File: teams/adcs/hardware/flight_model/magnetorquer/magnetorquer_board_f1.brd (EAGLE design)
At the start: 90 x 90 mm, 35 parts, among them U5 LTC3624

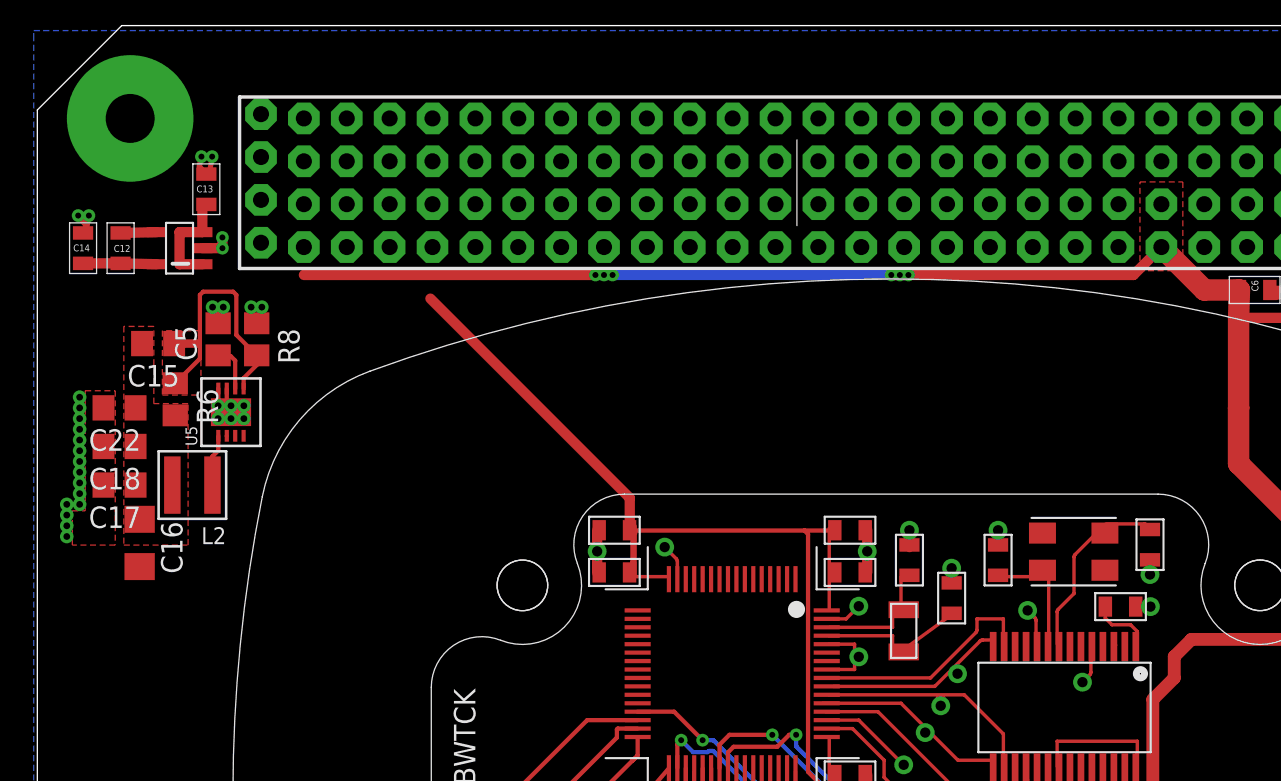
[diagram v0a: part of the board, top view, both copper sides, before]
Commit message: ADCS/MT: Reconnect CAN
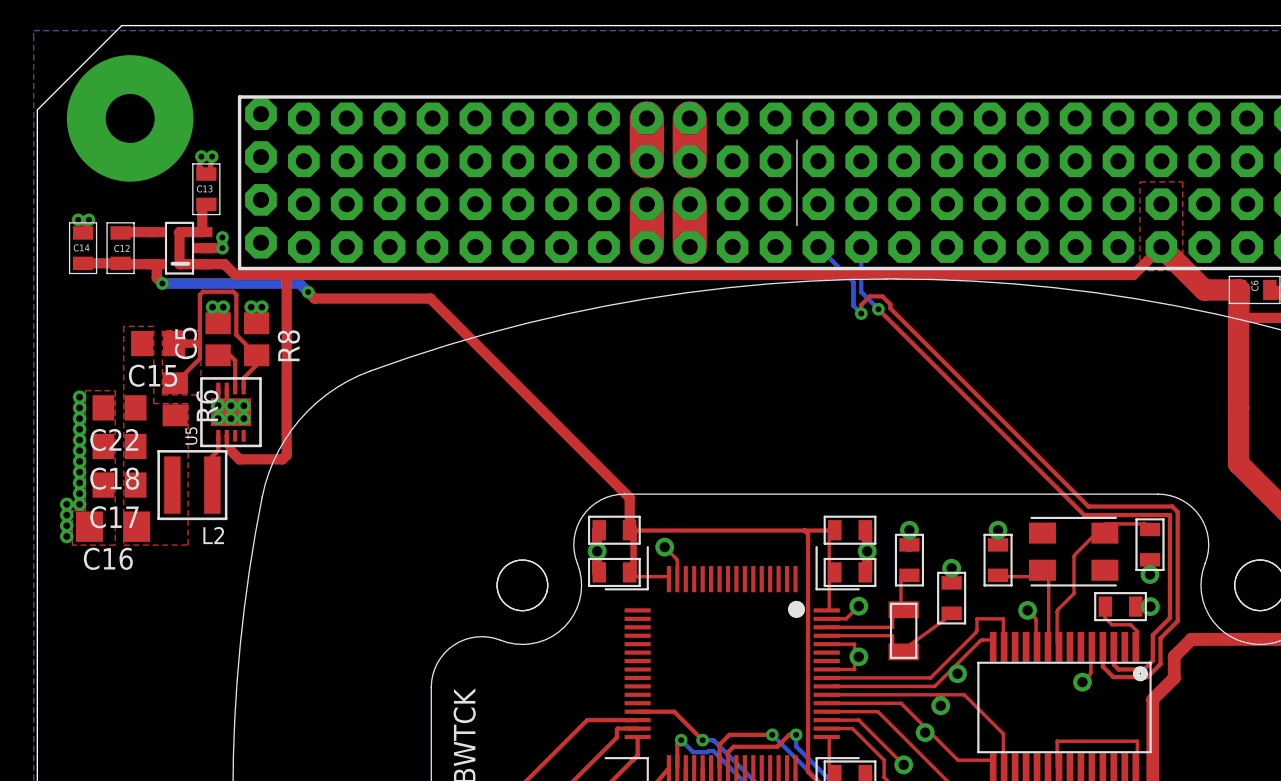
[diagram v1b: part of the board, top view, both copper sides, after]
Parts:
- moved C16 1.85 mm to (15.9, 59.0), turned to 180 degrees
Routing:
- net CANH: track 0.00 -> 44.5 mm, vias 0 -> 1
- net CANL: track 0.12 -> 39.3 mm, vias 0 -> 1
- net VBAT: track 110.9 -> 130.4 mm, vias 14 -> 8
- net +3V3: track 68.3 -> 85.8 mm, vias 0 -> 2
- net MT_Y_B: track 0.00 -> 2.54 mm
- net MT_Y_A: track 0.00 -> 2.54 mm
- net MT_X_B: track 0.00 -> 2.54 mm
- net MT_X_A: track 0.00 -> 2.54 mm

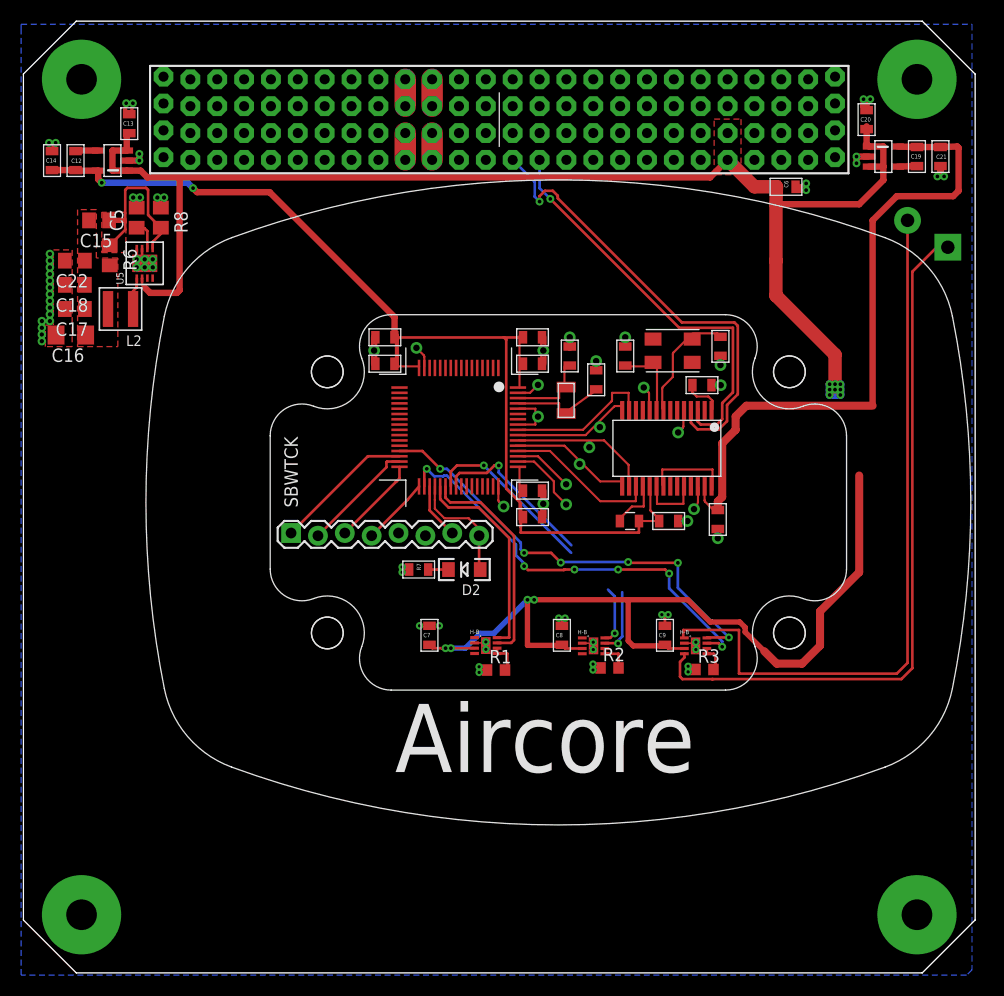
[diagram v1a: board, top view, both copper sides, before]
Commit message: ADCS/MT: Properly connect buck converter and reposition smoothing capacitors on H-Bridge
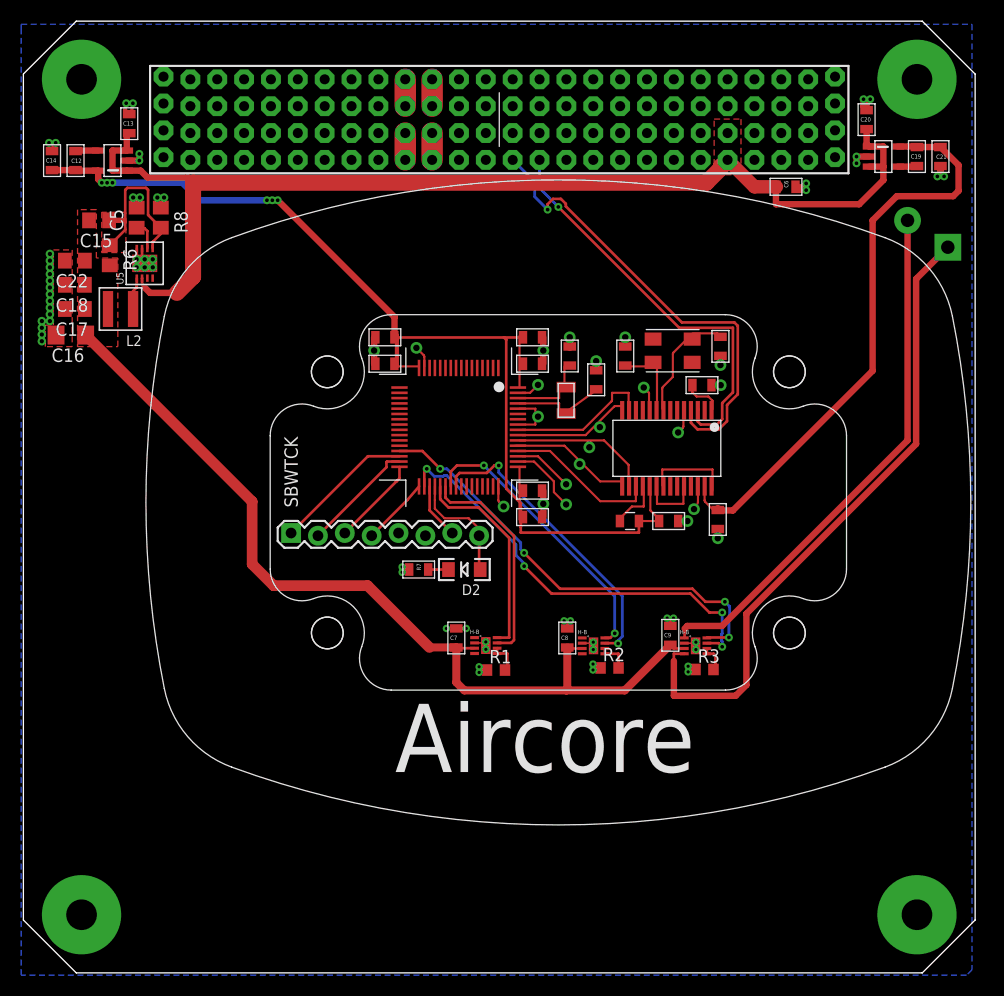
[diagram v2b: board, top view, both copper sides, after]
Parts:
- moved C7 2.55 mm to (52.3, 30.4)
- moved C8 0.57 mm to (62.8, 30.4)
- moved C9 0.51 mm to (72.6, 30.6)
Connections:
- removed net 3V3_BUCK_VOUT: C15.2, C16.1, C17.1, C18.1, C22.1, L2.P$2, R6.2
- net V_TORQ: now also C15.2, C16.1, C17.1, C18.1, C22.1, L2.P$2, R6.2
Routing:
- net VBAT: track 130.4 -> 106.3 mm, vias 8 -> 0
- net MT_Z_B: track 68.2 -> 50.2 mm
- net +5V: track 59.5 -> 52.8 mm
- net PWM_X_1: track 22.1 -> 28.5 mm
- net PWM_X_2: track 21.9 -> 26.9 mm
- net MT_Z_A: track 65.8 -> 61.6 mm
- net V_TORQ: track 82.2 -> 85.3 mm, vias 4 -> 0
- net PWM_Z_1: track 40.2 -> 41.0 mm, vias 6 -> 4
- net PWM_Z_2: track 42.4 -> 42.8 mm, vias 6 -> 4
- net +3V3: vias 2 -> 6
- added copper zone on layer 1, net V_TORQ
- removed copper zone on layer 1, net 3V3_BUCK_VOUT

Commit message: PC104 connector change: switched X and Y pin assignments, MQT board: converted to 4 layer board, layer 4 GND, previous layer 2 traces moved to new layer 2; added X and Y MQT outputs; added 3x LDOs
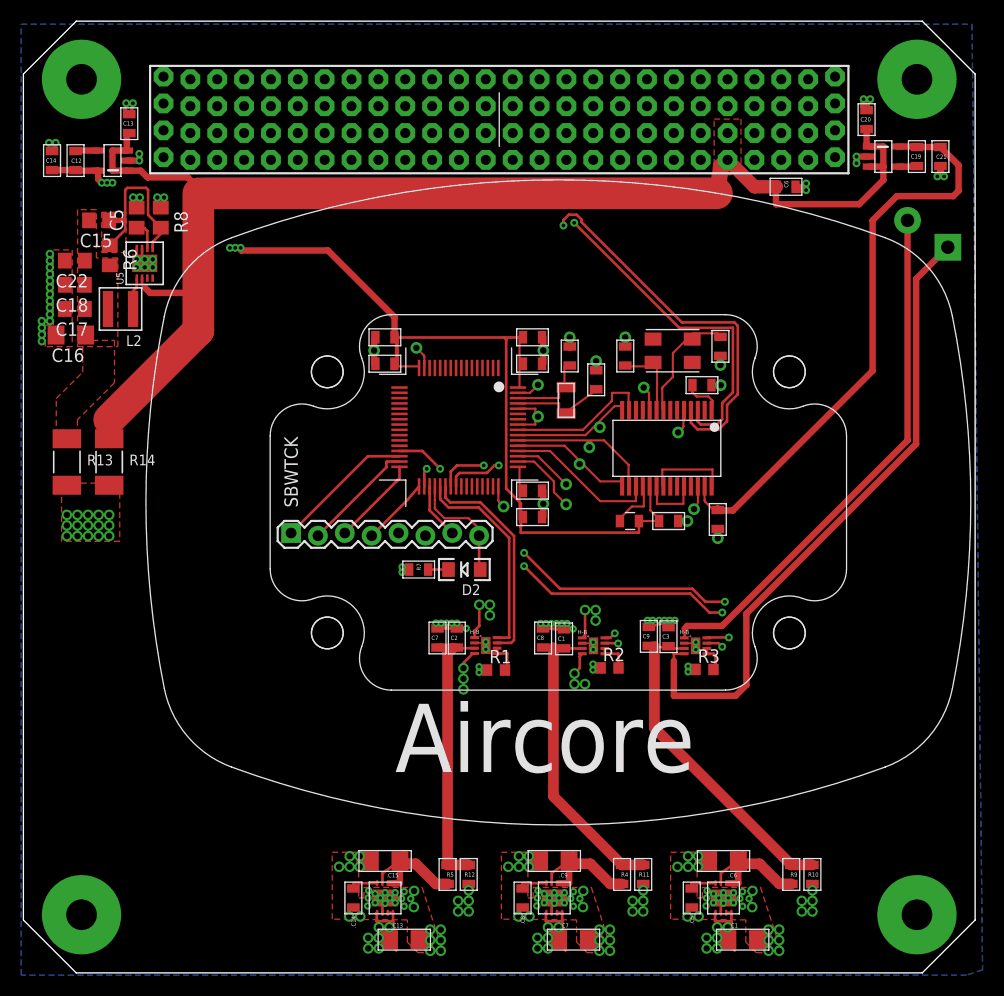
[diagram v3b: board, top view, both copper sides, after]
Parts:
- added .C1, .C13, .C15, .C6, .C7, .C9: 4.7u, SparkFun-Capacitors:1206
- added .C14, .C5, .C8: 10n, SparkFun-Capacitors:0805
- added C1, C2, C3: 1uF, DubSat1 Components:0805
- added R10, R11, R12: 0, DubSat1 Components:0805
- added R13: 0, DubSat1 Components:R2010
- added R14: DNP, DubSat1 Components:R2010
- added R4, R5, R9: DNP, DubSat1 Components:0805
- added U$4, U$5, U$9: ANALOG_LDO_ADM7172, ICs:8-LFCSP
- moved C8 2.29 mm to (60.5, 30.4)
- moved C9 2.03 mm to (70.5, 30.5)
- moved C7 1.78 mm to (50.5, 30.4)
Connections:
- removed net V_TORQ: C15.2, C16.1, C17.1, C18.1, C22.1, C7.2, C8.2, C9.2, L2.P$2, R6.2, U1.VDD, U2.VDD, U3.VDD
- new net N$11: .C8.1, U$5.P$4
- new net N$15: .C14.1, U$9.P$4
- new net N$9: .C5.1, U$4.P$4
- new net VBUCK: C15.2, C16.1, C17.1, C18.1, C22.1, L2.P$2, R13.1, R6.2
- new net VBUCK/VBAT: .C1.1, .C13.1, .C7.1, R10.1, R11.1, R12.1, R13.2, R14.2, U$4.P$5, U$4.P$7, U$4.P$8, U$5.P$5, U$5.P$7, U$5.P$8, U$9.P$5, U$9.P$7, U$9.P$8
- new net VOUT-X: .C9.1, R4.1, U$5.P$1, U$5.P$2, U$5.P$3
- new net VOUT-Y: .C15.1, R5.1, U$9.P$1, U$9.P$2, U$9.P$3
- new net VOUT-Z: .C6.1, R9.1, U$4.P$1, U$4.P$2, U$4.P$3
- new net V_TORQ-X: C1.2, C8.2, R11.2, R4.2, U2.VDD
- new net V_TORQ-Y: C2.2, C7.2, R12.2, R5.2, U1.VDD
- new net V_TORQ-Z: C3.2, C9.2, R10.2, R9.2, U3.VDD
- net GND: now also .C1.2, .C13.2, .C14.2, .C15.2, .C5.2, .C6.2, .C7.2, .C8.2, .C9.2, C1.1, C2.1, C3.1, U$4.P$6, U$4.P$9, U$5.P$6, U$5.P$9, U$9.P$6, U$9.P$9
- net MT_X_A: now also U$1.P$39, U$1.P$40; no longer U$1.P$37, U$1.P$38
- net MT_X_B: now also U$1.P$43, U$1.P$44; no longer U$1.P$41, U$1.P$42
- net MT_Y_A: now also U$1.P$37, U$1.P$38; no longer U$1.P$39, U$1.P$40
- net MT_Y_B: now also U$1.P$41, U$1.P$42; no longer U$1.P$43, U$1.P$44
- net VBAT: now also R14.1
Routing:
- net MT_Y_A: track 2.54 -> 92.3 mm, vias 0 -> 3
- net MT_Y_B: track 2.54 -> 88.5 mm, vias 0 -> 3
- net V_TORQ: track 85.3 -> 0.00 mm
- net MT_X_A: track 2.54 -> 73.6 mm, vias 0 -> 3
- net MT_X_B: track 2.54 -> 70.4 mm, vias 0 -> 3
- net V_TORQ-Z: track 0.00 -> 31.4 mm
- net V_TORQ-Y: track 0.00 -> 29.8 mm
- net V_TORQ-X: track 0.00 -> 28.9 mm
- net GND: track 38.0 -> 66.4 mm, vias 59 -> 162
- net VBUCK/VBAT: track 0.00 -> 23.0 mm, vias 0 -> 48
- net VBAT: track 106.3 -> 124.1 mm
- net VOUT-X: track 0.00 -> 14.3 mm
- net VOUT-Z: track 0.00 -> 14.3 mm
- net VOUT-Y: track 0.00 -> 13.2 mm
- net N$9: track 0.00 -> 2.75 mm
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- added copper zone on layer 3, net MT_X_A
- added copper zone on layer 2, net MT_X_B
- added copper zone on layer 1, net VBUCK
- added copper zone on layer 1, net VBUCK/VBAT
- added copper zone on layer 2, net VBUCK/VBAT
- removed copper zone on layer 1, net V_TORQ
